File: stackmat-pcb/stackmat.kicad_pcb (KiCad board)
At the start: 2 copper layers, 50 x 33.3 mm, 12 parts, among them U2 18650, U3 AMS1117-3.3

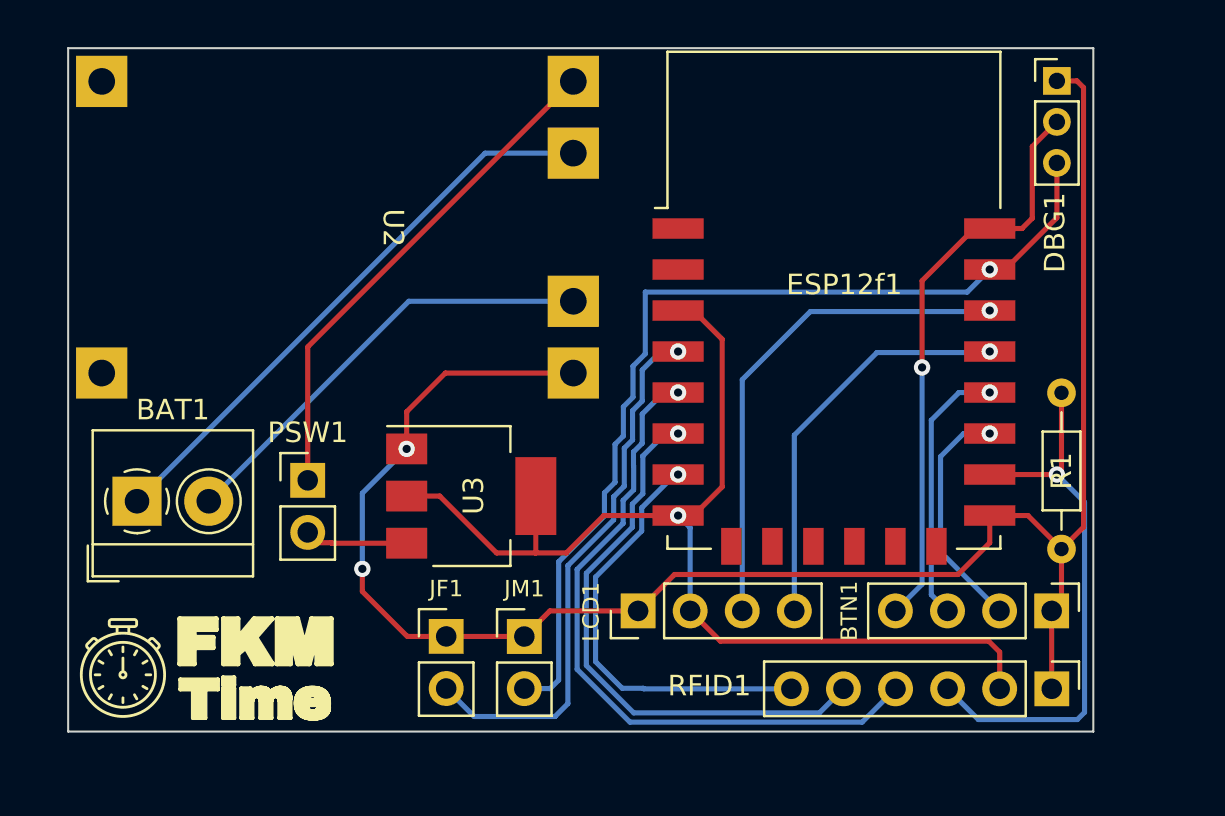
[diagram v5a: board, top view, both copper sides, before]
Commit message: wip(pcb): transistors instead of serial "copy"
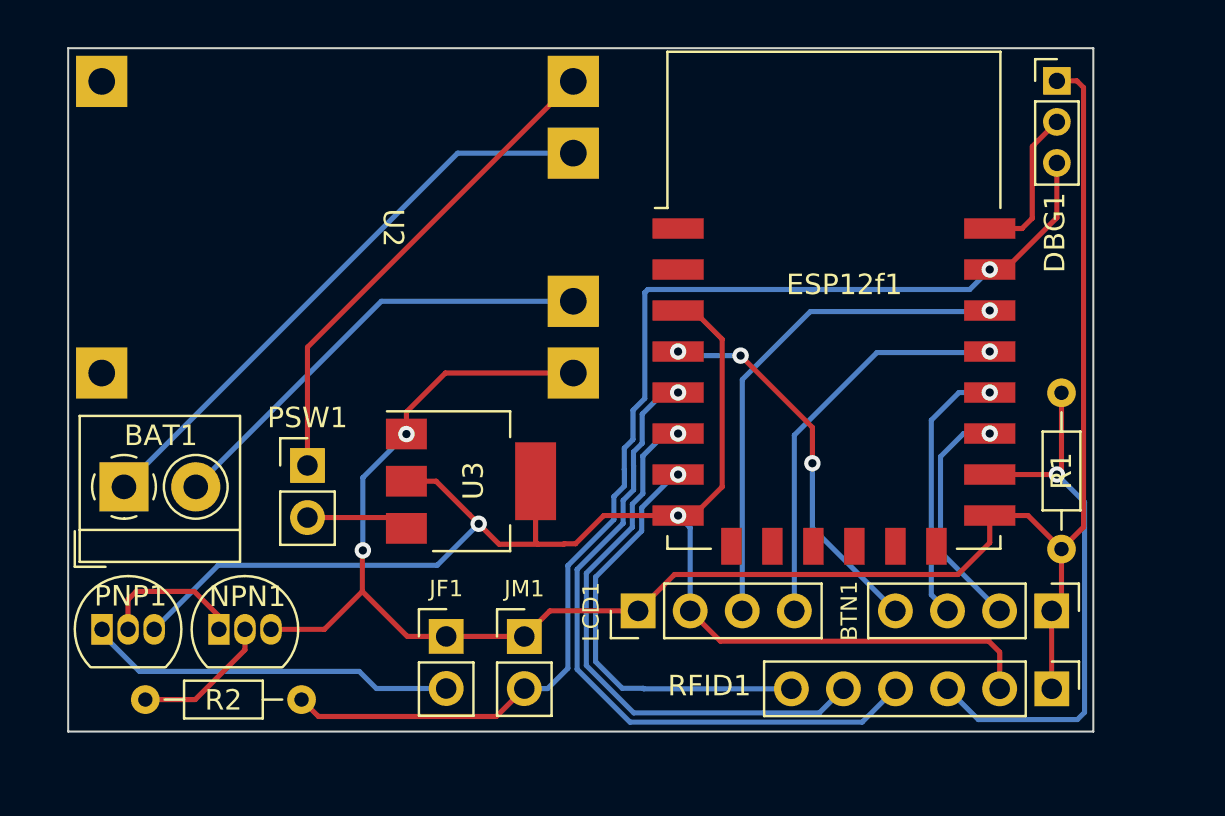
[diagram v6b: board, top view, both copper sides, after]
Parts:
- added NPN1: BC337, Package_TO_SOT_THT:TO-92_Inline, F.Cu at (74.2, 103.3)
- added PNP1: BC557, Package_TO_SOT_THT:TO-92_Inline, F.Cu at (68.5, 103.3)
- added R2: R100000, Resistor_THT:R_Axial_DIN0204_L3.6mm_D1.6mm_P7.62mm_Horizontal, F.Cu at (70.6, 106.7)
- moved BAT1 0.95 mm to (69.5, 96.3)
- moved PSW1 0.72 mm to (78.5, 95.3)
- moved U3 0.72 mm to (86.5, 96.0)
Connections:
- DBG1 pad 2: Net-(BTN1-Pin_4) -> Net-(DBG1-Pin_2)
- ESP12f1 pad 22: Net-(BTN1-Pin_4) -> Net-(DBG1-Pin_2)
- ESP12f1 pad 4: Net-(ESP12f1-GPIO16) -> Net-(BTN1-Pin_4)
- JF1 pad 2: Net-(ESP12f1-GPIO16) -> Net-(JF1-Pin_2)
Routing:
- net Net-(ESP12f1-GPIO16): track 26.7 -> 0.00 mm, vias 1 -> 0
- net +3.3V: track 53.2 -> 71.5 mm, vias 1 -> 2
- net Net-(JF1-Pin_2): track 0.00 -> 18.1 mm
- net Net-(DBG1-Pin_3): track 46.8 -> 58.5 mm
- net Net-(BTN1-Pin_4): track 28.5 -> 18.7 mm, vias 1 -> 3
- net Net-(DBG1-Pin_2): track 0.00 -> 8.23 mm
- net Net-(NPN1-C): track 0.00 -> 7.19 mm
- net Net-(NPN1-B): track 0.00 -> 6.86 mm
- net GND: track 89.0 -> 94.2 mm
- net Net-(PSW1-Pin_1): track 24.8 -> 24.1 mm

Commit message: feat(pcb): one transistor design
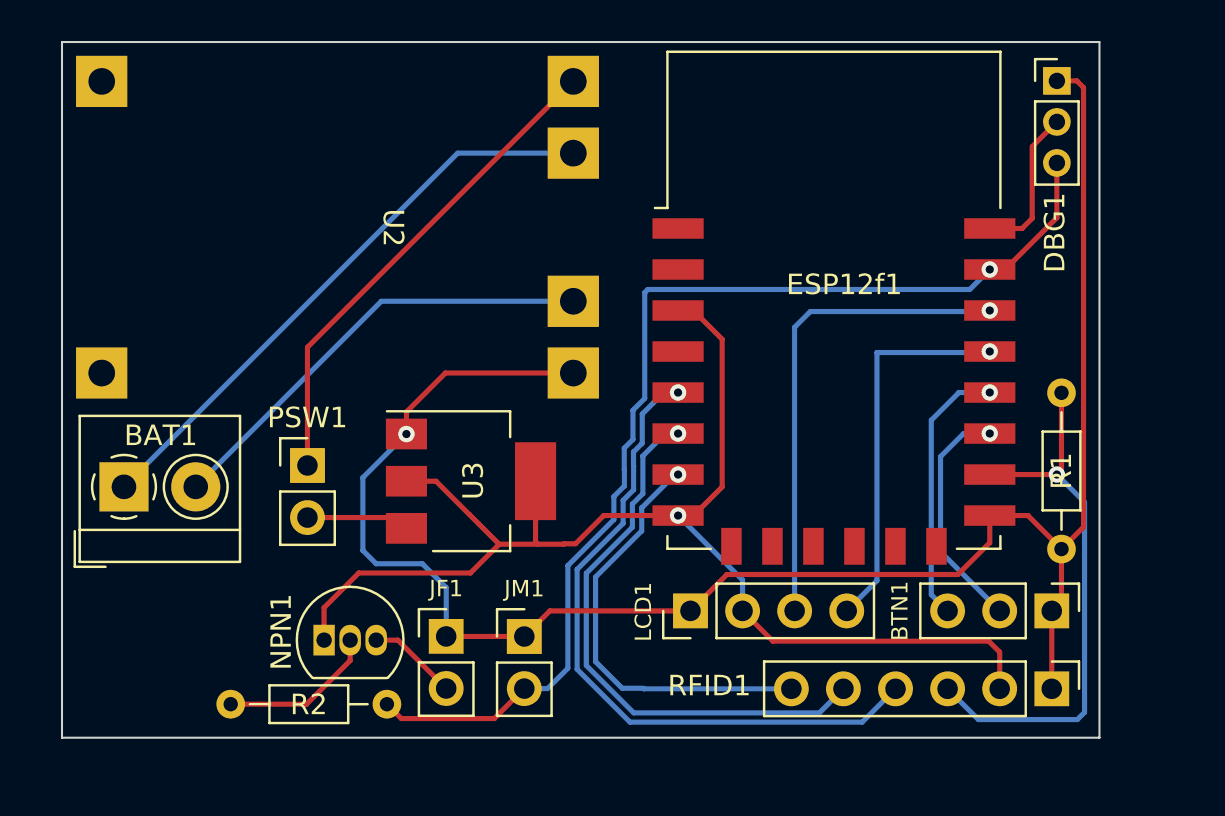
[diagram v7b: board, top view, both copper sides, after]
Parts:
- removed PNP1: BC557, Package_TO_SOT_THT:TO-92_Inline
- BTN1: value Conn_01x04 -> Conn_01x03; footprint Connector_PinHeader_2.54mm:PinHeader_1x04_P2.54mm_Vertical -> Connector_PinHeader_2.54mm:PinHeader_1x03_P2.54mm_Vertical
- moved NPN1 5.16 mm to (79.3, 103.8)
- moved R2 4.17 mm to (74.7, 106.9)
- moved LCD1 2.56 mm to (97.2, 102.4)
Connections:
- ESP12f1 pad 4: Net-(BTN1-Pin_4) -> unconnected-(ESP12f1-GPIO16-Pad4)
- NPN1 pad 1: Net-(NPN1-C) -> +3.3V
- NPN1 pad 3: GND -> Net-(JF1-Pin_2)
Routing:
- net Net-(BTN1-Pin_4): track 18.7 -> 0.00 mm, vias 3 -> 0
- net Net-(JF1-Pin_2): track 18.1 -> 4.97 mm
- net +3.3V: track 71.5 -> 63.4 mm, vias 2 -> 1
- net Net-(NPN1-C): track 7.19 -> 0.00 mm
- net GND: track 94.2 -> 89.4 mm, vias 2 -> 1
- net Net-(DBG1-Pin_3): track 58.5 -> 54.3 mm
- net Net-(ESP12f1-GPIO4): track 19.8 -> 18.7 mm
- net Net-(ESP12f1-GPIO5): track 24.7 -> 23.7 mm
- net Net-(NPN1-B): track 6.86 -> 7.71 mm
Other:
- board size 50 x 33.3 mm -> 50.6 x 33.9 mm

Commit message: feat: hardware based serial amplifier, better submit button
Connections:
- NPN1 pad 1: +3.3V -> Net-(JF1-Pin_2)
- NPN1 pad 3: Net-(JF1-Pin_2) -> +3.3V
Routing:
- net +3.3V: track 63.4 -> 59.9 mm
- net Net-(JF1-Pin_2): track 4.97 -> 7.48 mm
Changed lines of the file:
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@@
       (stroke (width 0.1) (type solid)) (layer "F.Fab"))
     (pad "1" thru_hole rect (at 0 0) (size 1.05 1.5) (drill 0.75) (layers "*.Cu" "*.Mask")
-      (net 22 "+3.3V") (pinfunction "C") (pintype "passive"))
+      (net 25 "Net-(JF1-Pin_2)") (pinfunction "C") (pintype "passive"))
     (pad "2" thru_hole oval (at 1.27 0) (size 1.05 1.5) (drill 0.75) (layers "*.Cu" "*.Mask")
       (net 27 "Net-(NPN1-B)") (pinfunction "B") (pintype "input"))
     (pad "3" thru_hole oval (at 2.54 0) (size 1.05 1.5) (drill 0.75) (layers "*.Cu" "*.Mask")
-      (net 25 "Net-(JF1-Pin_2)") (pinfunction "E") (pintype "passive"))
+      (net 22 "+3.3V") (pinfunction "E") (pintype "passive"))
     (model "${KICAD6_3DMODEL_DIR}/Package_TO_SOT_THT.3dshapes/TO-92_Inline.wrl"
       (offset (xyz 0 0 0))
@@
   (segment (start 96.55 87.725) (end 97.3 87.725) (width 0.25) (layer "F.Cu") (net 22))
   (segment (start 86.375 97.675) (end 86.825 98.125) (width 0.25) (layer "F.Cu") (net 22))
-  (segment (start 80.975 100.525) (end 79.285 102.215) (width 0.25) (layer "F.Cu") (net 22))
   (segment (start 90.975 99.125) (end 91 99.1) (width 0.25) (layer "F.Cu") (net 22))
   (segment (start 99.695 102.375) (end 101.17 103.85) (width 0.25) (layer "F.Cu") (net 22))
   (segment (start 86.825 98.125) (end 87.825 99.125) (width 0.25) (layer "F.Cu") (net 22))
   (segment (start 86.425 100.525) (end 87.825 99.125) (width 0.25) (layer "F.Cu") (net 22))
-  (segment (start 80.975 100.525) (end 86.425 100.525) (width 0.25) (layer "F.Cu") (net 22))
-  (segment (start 79.285 102.215) (end 79.285 103.8) (width 0.25) (layer "F.Cu") (net 22))
   (segment (start 92.925 97.725) (end 96.55 97.725) (width 0.25) (layer "F.Cu") (net 22))
   (segment (start 91 99.1) (end 91.55 99.1) (width 0.25) (layer "F.Cu") (net 22))
@@
   (segment (start 89.6 96.05) (end 89.6 99.025) (width 0.25) (layer "F.Cu") (net 22))
   (segment (start 101.17 103.85) (end 111.7 103.85) (width 0.25) (layer "F.Cu") (net 22))
+  (segment (start 81.825 103.8) (end 85.1 100.525) (width 0.25) (layer "F.Cu") (net 22))
   (segment (start 87.825 99.125) (end 89.7 99.125) (width 0.25) (layer "F.Cu") (net 22))
   (segment (start 111.7 103.85) (end 112.235 104.385) (width 0.25) (layer "F.Cu") (net 22))
+  (segment (start 85.1 100.525) (end 86.425 100.525) (width 0.25) (layer "F.Cu") (net 22))
   (segment (start 89.7 99.125) (end 90.975 99.125) (width 0.25) (layer "F.Cu") (net 22))
   (segment (start 84.75 96.05) (end 86.375 97.675) (width 0.25) (layer "F.Cu") (net 22))
@@
   (segment (start 78.474 97.823) (end 82.773 97.823) (width 0.25) (layer "F.Cu") (net 24))
   (segment (start 82.773 97.823) (end 83.3 98.35) (width 0.25) (layer "F.Cu") (net 24))
-  (segment (start 82.88 103.8) (end 85.24 106.16) (width 0.25) (layer "F.Cu") (net 25))
-  (segment (start 81.825 103.8) (end 82.88 103.8) (width 0.25) (layer "F.Cu") (net 25))
-  (segment (start 85.24 106.16) (end 84.83 105.75) (width 0.25) (layer "B.Cu") (net 25))
+  (segment (start 79.85 105.3) (end 79.285 104.735) (width 0.25) (layer "B.Cu") (net 25))
+  (segment (start 85.24 106.16) (end 84.38 105.3) (width 0.25) (layer "B.Cu") (net 25))
+  (segment (start 84.38 105.3) (end 79.85 105.3) (width 0.25) (layer "B.Cu") (net 25))
+  (segment (start 79.285 104.735) (end 79.285 103.8) (width 0.25) (layer "B.Cu") (net 25))
   (segment (start 80.555 104.8) (end 78.43 106.925) (width 0.25) (layer "F.Cu") (net 27))
   (segment (start 78.43 106.925) (end 74.73 106.925) (width 0.25) (layer "F.Cu") (net 27))
